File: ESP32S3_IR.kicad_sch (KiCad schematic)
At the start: 11 parts, among them J1 ESP32_Right, J2 ESP32_Left, J3 I2C, SW1 C318938, SW2 C318938, SW3 C318938

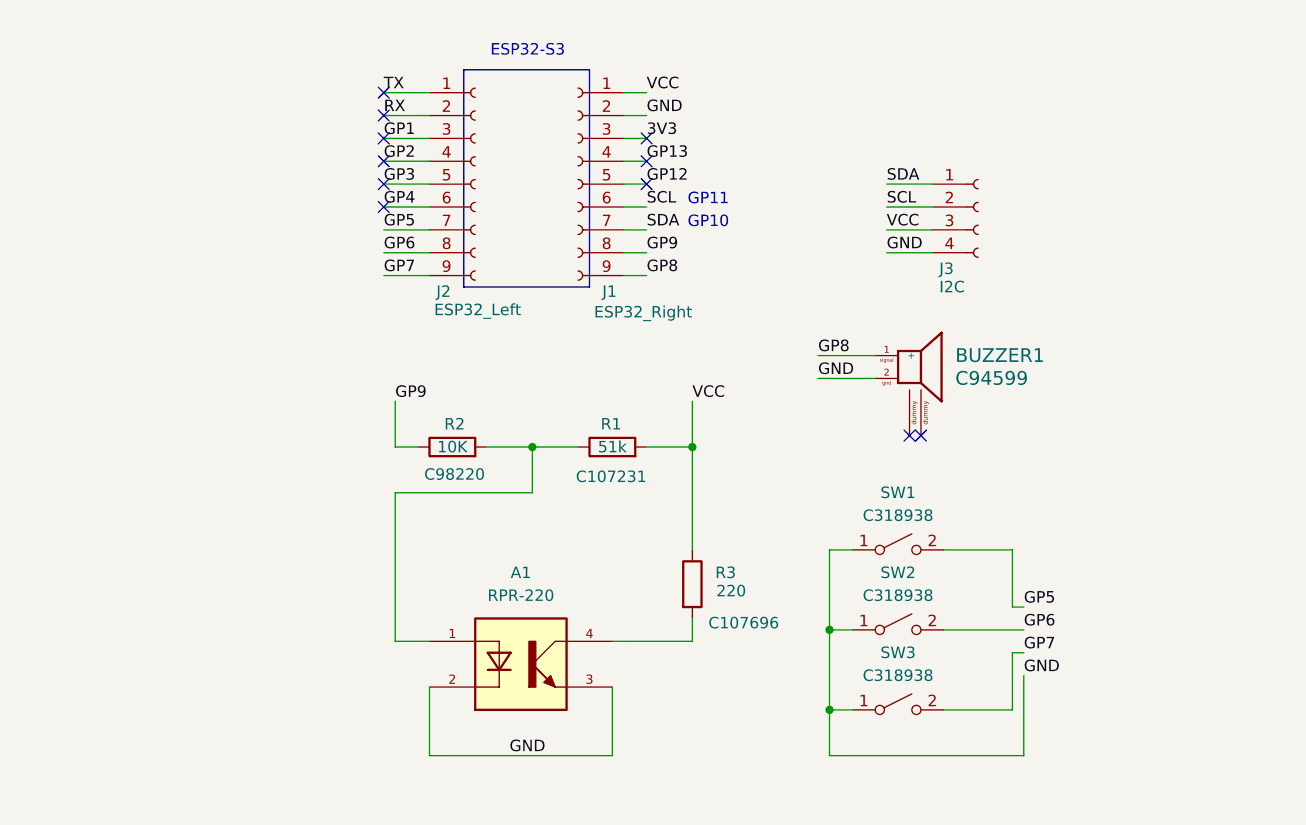
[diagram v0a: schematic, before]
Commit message: update buzzer->5V
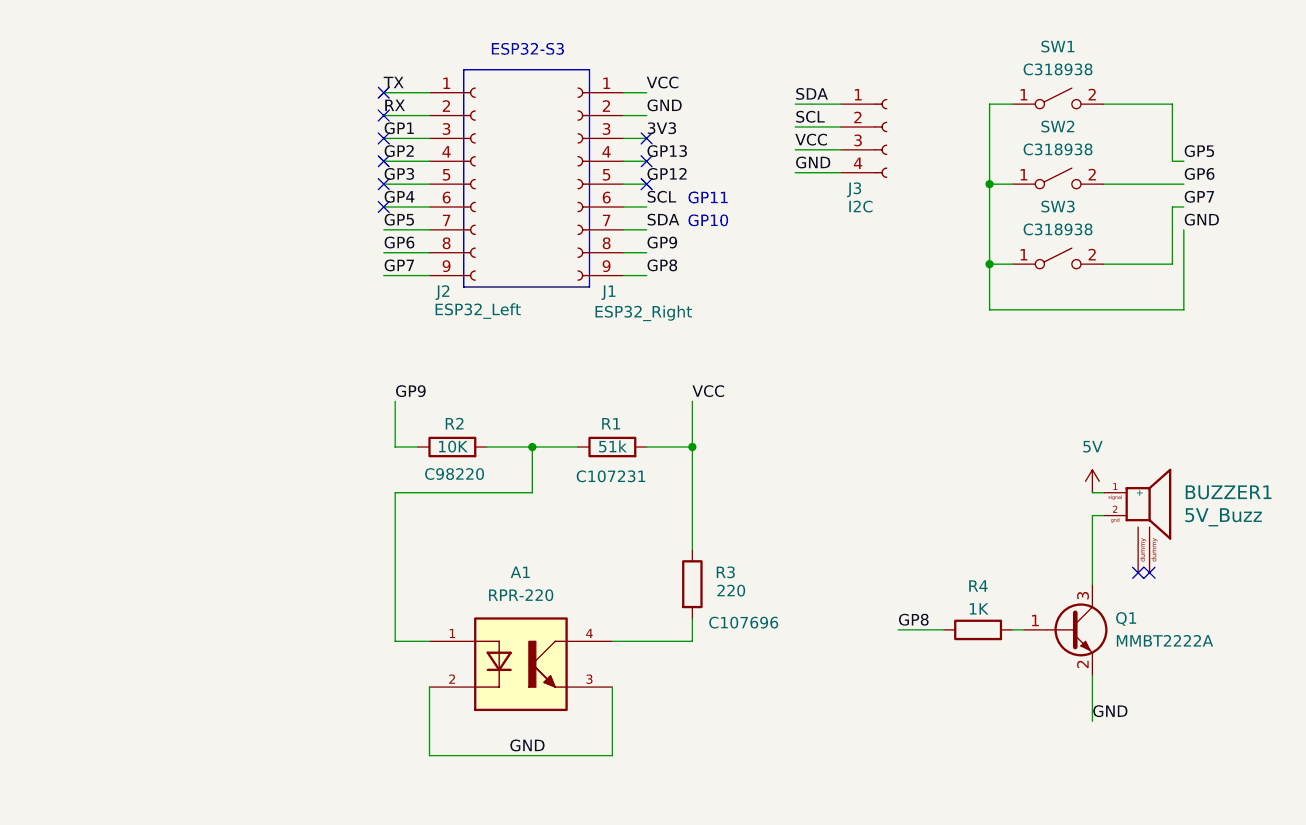
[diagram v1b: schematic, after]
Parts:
- added Q1: MMBT2222A, Package_TO_SOT_SMD:SOT-23, symbol Transistor_BJT:MMBT2222A
- added R4: 1K, symbol Device:R
- BUZZER1: value C94599 -> 5V_Buzz
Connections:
- net GND: now also Q1.2 (E); no longer BUZZER1.2
- net GP8: now also R4.1; no longer BUZZER1.1 (+)
- new net: Q1.1 (B), R4.2
- new net: BUZZER1.2, Q1.3 (C)
- new net 5V: BUZZER1.1 (+)
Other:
- moved on the sheet: BUZZER1, J3, SW1, SW2, SW3

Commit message: update SCH: add battery sensor ADC  & split net into 3V3 & 5V powerline.
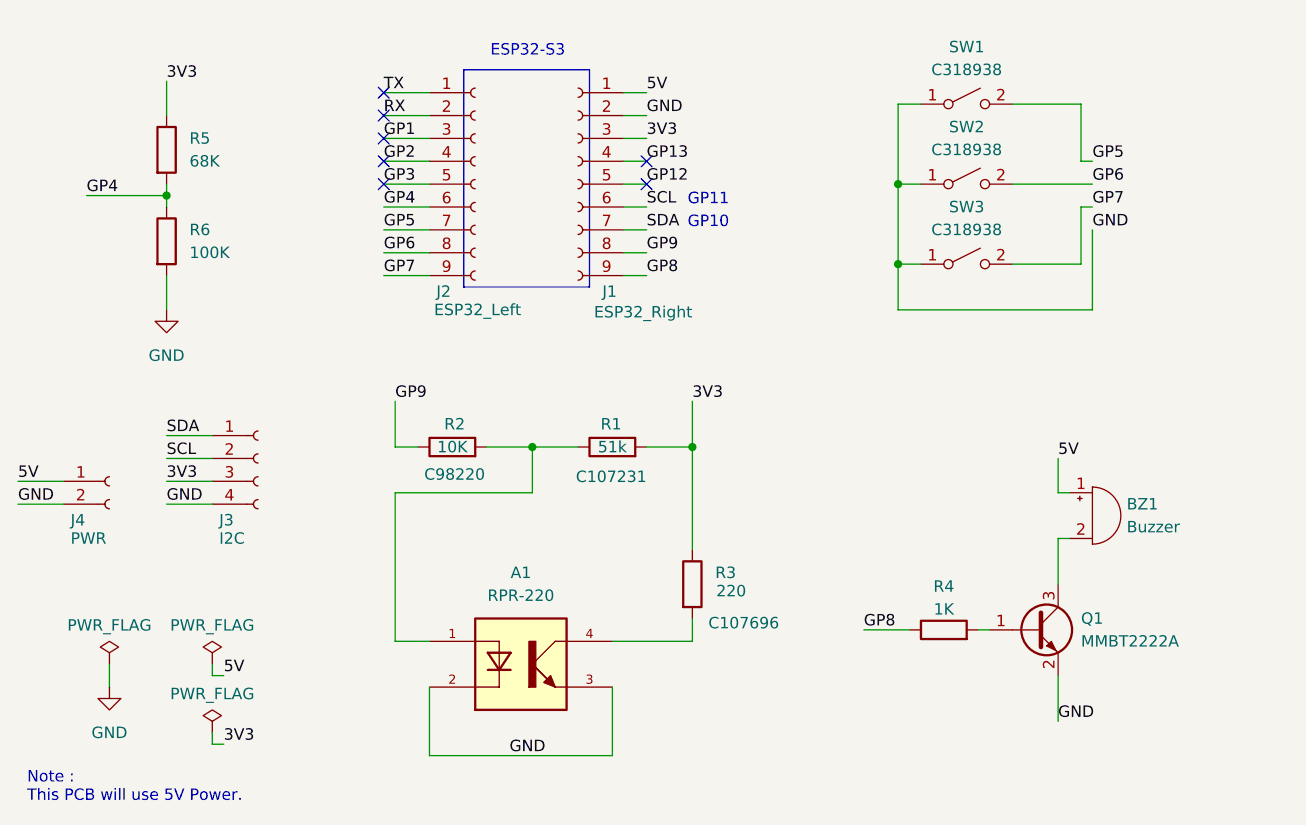
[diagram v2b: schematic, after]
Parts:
- removed BUZZER1: 5V_Buzz, Buzzer_Beeper:MLT-8530, symbol Device:MLT-8530
- added BZ1: Buzzer, Buzzer_Beeper:Buzzer_12x9.5RM7.6, symbol Device:Buzzer
- added J4: PWR, Connector_PinSocket_2.54mm:PinSocket_1x02_P2.54mm_Vertical, symbol Connector:Conn_01x02_Socket
- added R5: 68K, Resistor_SMD:R_0603_1608Metric, symbol Device:R
- added R6: 100K, Resistor_SMD:R_0603_1608Metric, symbol Device:R
- R4: footprint (none) -> Resistor_SMD:R_0603_1608Metric
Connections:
- net 3V3: now also J3.3 (Pin_3), R1.2, R3.1, R5.1
- net 5V: now also J1.1 (Pin_1), BZ1.1 (+), J4.1 (Pin_1)
- net GND: now also J4.2 (Pin_2), R6.2
- net GP4: now also R5.2, R6.1
- net at Q1.3 (C): now also BZ1.2 (-)
- removed net VCC: J1.1 (Pin_1), J3.3 (Pin_3), R1.2, R3.1
- no-connect marks 11 -> 7
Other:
- note added: "Note : This PCB will use 5V Power."
- moved on the sheet: J3, Q1, R4, SW1, SW2, SW3

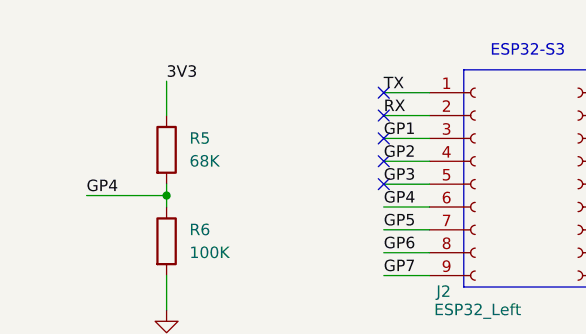
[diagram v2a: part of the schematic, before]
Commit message: change ADC sensor pin 3V3 -> BAT socket
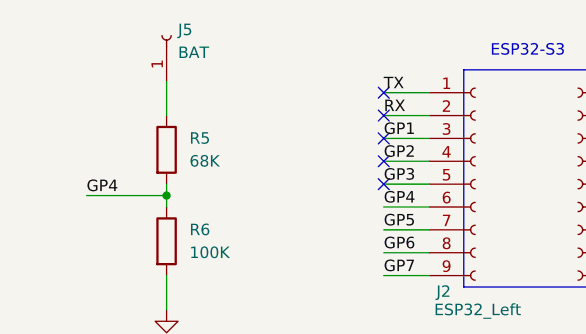
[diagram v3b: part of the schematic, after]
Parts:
- added J5: BAT, Connector_PinSocket_2.54mm:PinSocket_1x01_P2.54mm_Vertical, symbol Connector:Conn_01x01_Socket
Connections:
- net 3V3: no longer R5.1
- new net: J5.1 (Pin_1), R5.1
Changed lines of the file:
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@@
-	)
-	(label "3V3"
-		(at 95.25 36.83 0)
-		(effects
-			(font
-				(size 1.27 1.27)
-			)
-			(justify left bottom)
-		)
 	)
 	(label "3V3"
@@
 					(unit 1)
 				)
+			)
+		)
+	)
+	(symbol
+		(lib_id "Connector:Conn_01x01_Socket")
+		(at 95.25 31.75 90)
+		(unit 1)
+		(exclude_from_sim no)
+		(in_bom yes)
+		(on_board yes)
+		(dnp no)
+		(fields_autoplaced yes)
+		(property "Reference" "J5"
+			(at 96.52 31.1149 90)
+			(effects
+				(font
+					(size 1.27 1.27)
+				)
+				(justify right)
+			)
+		)
+		(property "Value" "BAT"
+			(at 96.52 33.6549 90)
+			(effects
+				(font
+					(size 1.27 1.27)
+				)
+				(justify right)
+			)
+		)
+		(property "Footprint" "Connector_PinSocket_2.54mm:PinSocket_1x01_P2.54mm_Vertical"
+			(at 95.25 31.75 0)
+			(effects
+				(font
+					(size 1.27 1.27)
+				)
+				(hide yes)
+			)
+		)
+		(property "Datasheet" "~"
+			(at 95.25 31.75 0)
+			(effects
+				(font
+					(size 1.27 1.27)
+				)
+				(hide yes)
+			)
+		)
+		(property "Description" "Generic connector, single row, 01x01, script generated"
+			(at 95.25 31.75 0)
+			(effects
+				(font
+					(size 1.27 1.27)
+				)
+				(hide yes)
+			)
+		)
+		(pin "1"
+		)
+		(instances
+			(project ""
+				(path "/02a9f5b4-4771-4986-a918-f0c534ed4c76"
+					(reference "J5")
+					(unit 1)
+				)

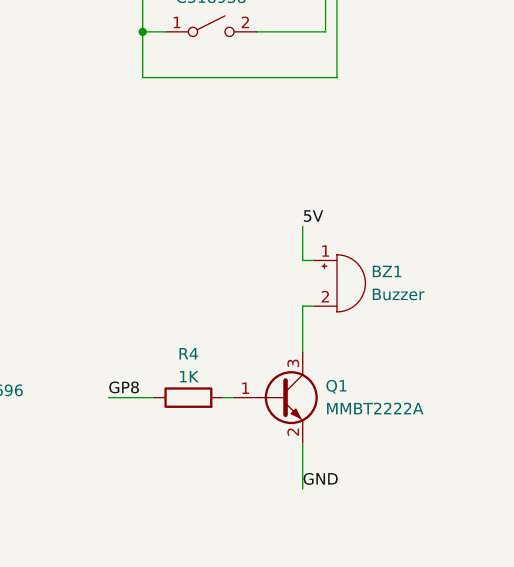
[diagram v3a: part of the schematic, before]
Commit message: Change Layout-> Fit Early THT requirement
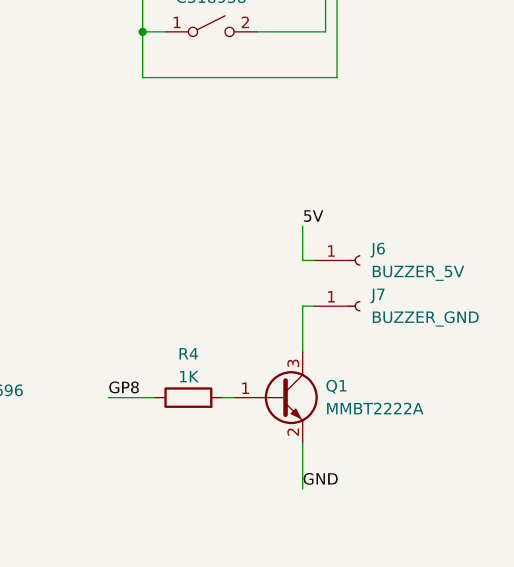
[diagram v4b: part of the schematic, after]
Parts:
- removed BZ1: Buzzer, Buzzer_Beeper:Buzzer_12x9.5RM7.6, symbol Device:Buzzer
- added J6: BUZZER_5V, Connector_PinSocket_2.54mm:PinSocket_1x01_P2.54mm_Vertical, symbol Connector:Conn_01x01_Socket
- added J7: BUZZER_GND, Connector_PinSocket_2.54mm:PinSocket_1x01_P2.54mm_Vertical, symbol Connector:Conn_01x01_Socket
- SW1, SW2, SW3: footprint Button_Switch_SMD:SW_SPST_CK_RS282G05A3 -> Button_Switch_THT:SW_PUSH_6mm
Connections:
- net 5V: now also J6.1 (Pin_1)
- net at Q1.3 (C): now also J7.1 (Pin_1)
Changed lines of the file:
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@@
+	)
+	(symbol
+		(lib_id "Connector:Conn_01x01_Socket")
+		(at 200.66 82.55 0)
+		(unit 1)
+		(exclude_from_sim no)
+		(in_bom yes)
+		(on_board yes)
+		(dnp no)
+		(fields_autoplaced yes)
+		(property "Reference" "J6"
+			(at 201.93 81.2799 0)
+			(effects
+				(font
+					(size 1.27 1.27)
+				)
+				(justify left)
+			)
+		)
+		(property "Value" "BUZZER_5V"
+			(at 201.93 83.8199 0)
+			(effects
+				(font
+					(size 1.27 1.27)
+				)
+				(justify left)
+			)
+		)
+		(property "Footprint" "Connector_PinSocket_2.54mm:PinSocket_1x01_P2.54mm_Vertical"
+			(at 200.66 82.55 0)
+			(effects
+				(font
+					(size 1.27 1.27)
+				)
+				(hide yes)
+			)
+		)
+		(property "Datasheet" "~"
+			(at 200.66 82.55 0)
+			(effects
+				(font
+					(size 1.27 1.27)
+				)
+				(hide yes)
+			)
+		)
+		(property "Description" "Generic connector, single row, 01x01, script generated"
+			(at 200.66 82.55 0)
+			(effects
+				(font
+					(size 1.27 1.27)
+				)
+				(hide yes)
+			)
+		)
+		(pin "1"
+		)
+		(instances
+			(project "ESP32S3_IR"
+				(path "/02a9f5b4-4771-4986-a918-f0c534ed4c76"
+					(reference "J6")
+					(unit 1)
+				)
+			)
+		)
 	)
 	(symbol
@@
 			)
 		)
-		(property "Footprint" "Button_Switch_SMD:SW_SPST_CK_RS282G05A3"
+		(property "Footprint" "Button_Switch_THT:SW_PUSH_6mm"
 			(at 184.15 57.15 0)
 			(effects
@@
 			)
 		)
-		(property "Footprint" "Button_Switch_SMD:SW_SPST_CK_RS282G05A3"
+		(property "Footprint" "Button_Switch_THT:SW_PUSH_6mm"
 			(at 184.15 39.37 0)
 			(effects
@@
 	)
 	(symbol
+		(lib_id "Connector:Conn_01x01_Socket")
+		(at 200.66 87.63 0)
+		(unit 1)
+		(exclude_from_sim no)
+		(in_bom yes)
+		(on_board yes)
+		(dnp no)
+		(fields_autoplaced yes)
+		(property "Reference" "J7"
+			(at 201.93 86.3599 0)
+			(effects
+				(font
+					(size 1.27 1.27)
+				)
+				(justify left)
+			)
+		)
+		(property "Value" "BUZZER_GND"
+			(at 201.93 88.8999 0)
+			(effects
+				(font
+					(size 1.27 1.27)
+				)
+				(justify left)
+			)
+		)
+		(property "Footprint" "Connector_PinSocket_2.54mm:PinSocket_1x01_P2.54mm_Vertical"
+			(at 200.66 87.63 0)
+			(effects
+				(font
+					(size 1.27 1.27)
+				)
+				(hide yes)
+			)
+		)
+		(property "Datasheet" "~"
+			(at 200.66 87.63 0)
+			(effects
+				(font
+					(size 1.27 1.27)
+				)
+				(hide yes)
+			)
+		)
+		(property "Description" "Generic connector, single row, 01x01, script generated"
+			(at 200.66 87.63 0)
+			(effects
+				(font
+					(size 1.27 1.27)
+				)
+				(hide yes)
+			)
+		)
+		(pin "1"
+		)
+		(instances
+			(project "ESP32S3_IR"
+				(path "/02a9f5b4-4771-4986-a918-f0c534ed4c76"
+					(reference "J7")
+					(unit 1)
+				)
+			)
+		)
+	)
+	(symbol
 		(lib_id "power:PWR_FLAG")
 		(at 100.33 101.6 0)
@@
 				(path "/02a9f5b4-4771-4986-a918-f0c534ed4c76"
 					(reference "#FLG02")
-					(unit 1)
-				)
-			)
-		)
-	)
-	(symbol
-		(lib_id "Device:Buzzer")
-		(at 198.12 85.09 0)
-		(unit 1)
-		(exclude_from_sim no)
-		(in_bom yes)
-		(on_board yes)
-		(dnp no)
-		(fields_autoplaced yes)
-		(property "Reference" "BZ1"
-			(at 201.93 83.8199 0)
-			(effects
-				(font
-					(size 1.27 1.27)
-				)
-				(justify left)
-			)
-		)
-		(property "Value" "Buzzer"
-			(at 201.93 86.3599 0)
-			(effects
-				(font
-					(size 1.27 1.27)
-				)
-				(justify left)
-			)
-		)
-		(property "Footprint" "Buzzer_Beeper:Buzzer_12x9.5RM7.6"
-			(at 197.485 82.55 90)
-			(effects
-				(font
-					(size 1.27 1.27)
-				)
-				(hide yes)
-			)
-		)
-		(property "Datasheet" "~"
-			(at 197.485 82.55 90)
-			(effects
-				(font
-					(size 1.27 1.27)
-				)
-				(hide yes)
-			)
-		)
-		(property "Description" "Buzzer, polarized"
-			(at 198.12 85.09 0)
-			(effects
-				(font
-					(size 1.27 1.27)
-				)
-				(hide yes)
-			)
-		)
-		(pin "1"
-		)
-		(pin "2"
-		)
-		(instances
-			(project ""
-				(path "/02a9f5b4-4771-4986-a918-f0c534ed4c76"
-					(reference "BZ1")
 					(unit 1)
 				)
@@
 			)
 		)
-		(property "Footprint" "Button_Switch_SMD:SW_SPST_CK_RS282G05A3"
+		(property "Footprint" "Button_Switch_THT:SW_PUSH_6mm"
 			(at 184.15 48.26 0)
 			(effects
